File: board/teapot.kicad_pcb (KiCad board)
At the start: 2 copper layers, 49.9 x 50 mm, 47 parts, among them J1 MICROUSB, P1 BATT, P2 SMA, Q1 TEPT4400, U1 TPS79333DBVR, U2 TLV61225, U4 RFM69W, U5 STM32L052K8, U6 HTU21D, U7 MS5637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

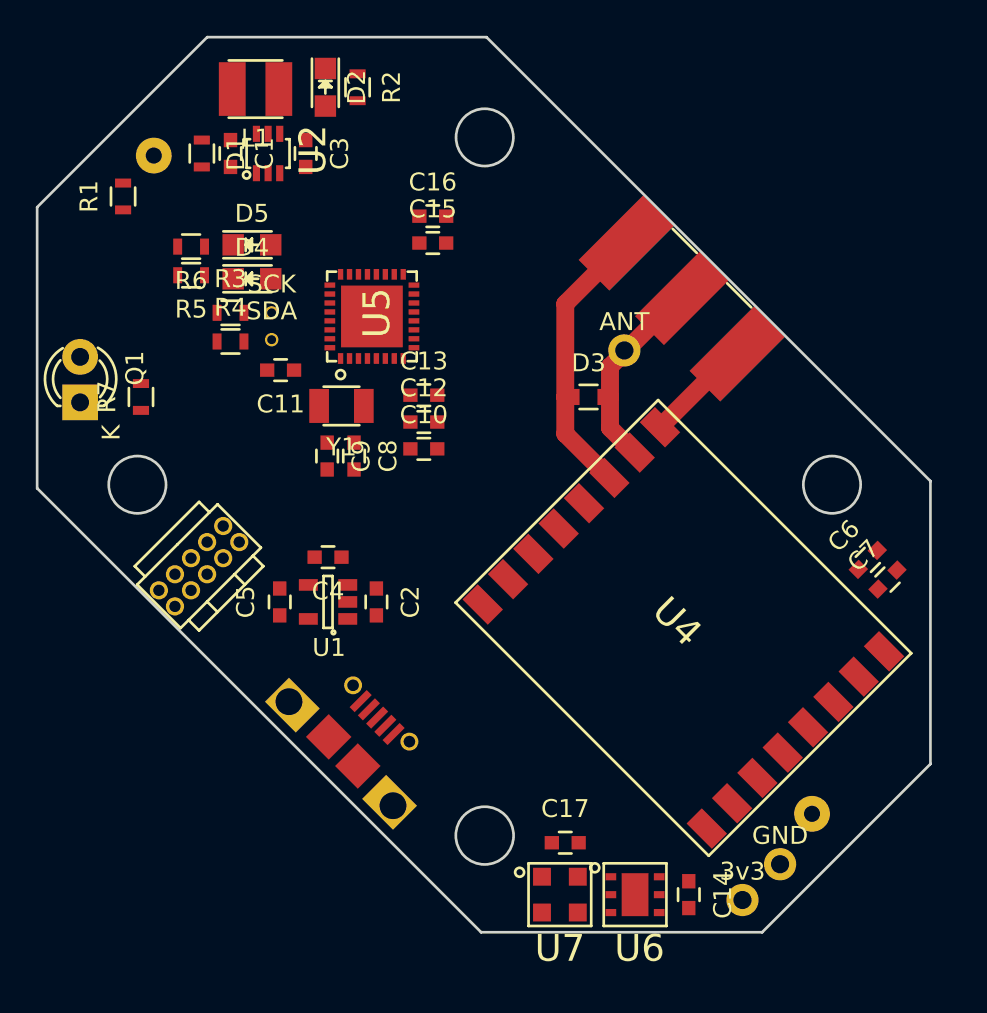
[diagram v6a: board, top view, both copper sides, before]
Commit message: layout switcher psu
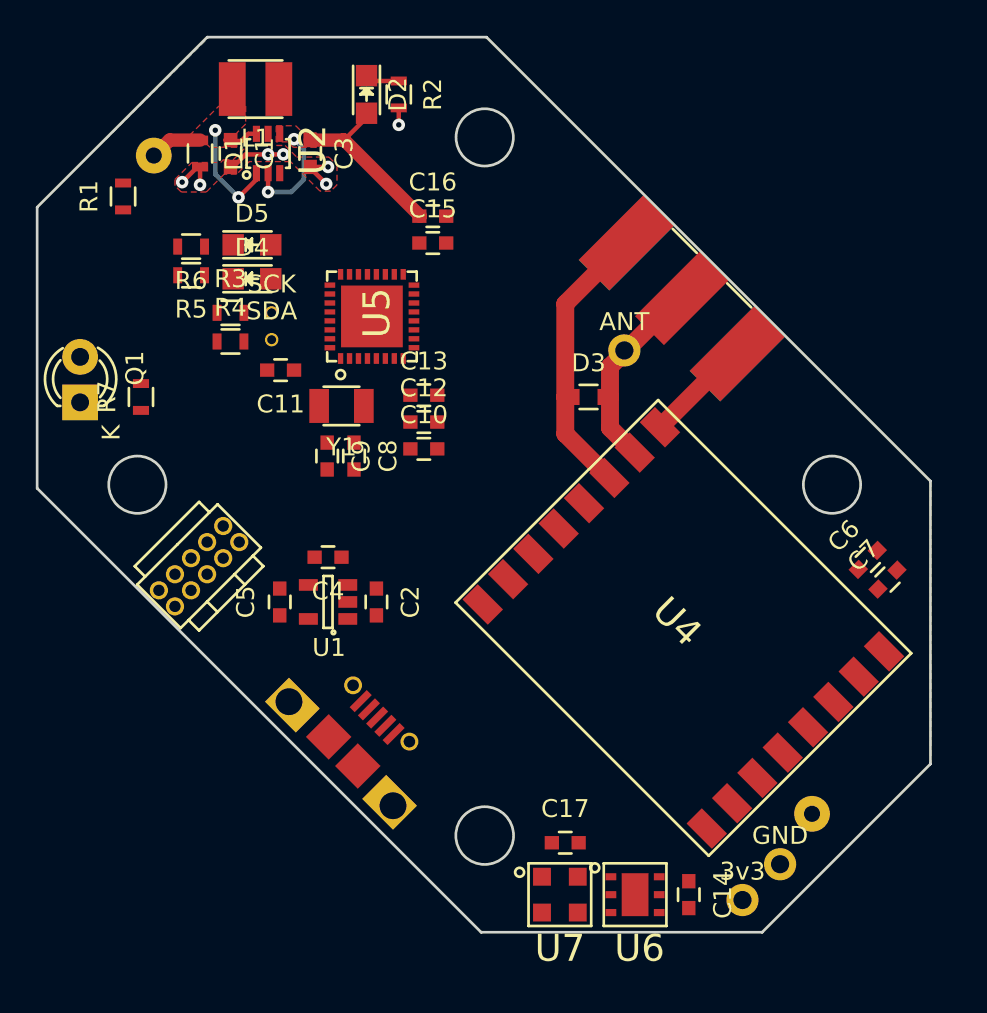
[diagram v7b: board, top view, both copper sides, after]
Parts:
- moved D2 2.33 mm to (120.4, 91.2)
- moved R2 2.33 mm to (122.2, 91.2)
- moved C3 0.25 mm to (117.2, 94.5)
- moved D1 0.10 mm to (111.1, 94.5)
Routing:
- net +3V3: track 0.00 -> 16.1 mm, vias 0 -> 2
- net Net-(C1-Pad1): track 0.00 -> 11.0 mm, vias 0 -> 2
- net GND: track 22.4 -> 31.3 mm, vias 0 -> 7
- net Net-(D2-Pad1): track 0.00 -> 2.47 mm
- added copper zone on F.Cu, net +3V3
- added copper zone on B.Cu, net GND
- added copper zone on F.Cu, net GND
- added copper zone on F.Cu, net Net-(C1-Pad1)
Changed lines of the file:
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@@
   (general
     (links 116)
-    (no_connects 111)
+    (no_connects 92)
     (area 101.924999 87.924999 151.975001 138.075001)
     (thickness 1.6)
     (drawings 16)
-    (tracks 17)
+    (tracks 73)
     (zones 0)
     (modules 47)
@@
     (user_trace_width 1)
     (trace_clearance 0.15)
-    (zone_clearance 0.5)
-    (zone_45_only no)
+    (zone_clearance 0.1)
+    (zone_45_only yes)
     (trace_min 0.2)
     (segment_width 0.2)
@@
   )
   (module Resistors_SMD:R_0603 (layer F.Cu)
-    (at 111.2 94.5 270)
+    (at 111.1 94.5 270)
     (descr "Resistor SMD 0603, reflow soldering, Vishay (see dcrcw.pdf)")
     (tags "resistor 0603")
@@
   )
   (module Capacitors_SMD:C_0603 (layer F.Cu)
-    (at 117 94.5 270)
+    (at 117.25 94.5 270)
     (descr "Capacitor SMD 0603, reflow soldering, AVX (see smccp.pdf)")
     (tags "capacitor 0603")
@@
   )
   (module LEDs:LED-0805 (layer F.Cu)
-    (at 118.1 90.8 270)
+    (at 120.4 91.2 270)
     (descr "LED 0805 smd package")
     (tags "LED 0805 SMD")
@@
   )
   (module Resistors_SMD:R_0603 (layer F.Cu)
-    (at 119.9 90.8 270)
+    (at 122.2 91.2 270)
     (descr "Resistor SMD 0603, reflow soldering, Vishay (see dcrcw.pdf)")
     (tags "resistor 0603")
@@
   (gr_circle (center 107.6 113) (end 109.2 113) (layer Edge.Cuts) (width 0.15))
   (gr_line (start 111.5 88) (end 102 97.5) (angle 90) (layer Edge.Cuts) (width 0.15))
+  (segment (start 120.4 92.24902) (end 120.4 92.5) (width 0.25) (layer F.Cu) (net 1) (status C00000))
+  (segment (start 120.4 92.5) (end 119.1 93.8) (width 0.25) (layer F.Cu) (net 1) (status 400000))
+  (segment (start 119.1 93.8) (end 119.1 93.75) (width 0.25) (layer F.Cu) (net 1))
+  (segment (start 120.3 92.3) (end 120.35 92.19902) (width 0.25) (layer F.Cu) (net 1))
+  (segment (start 117.25 93.75) (end 119.1 93.75) (width 0.75) (layer F.Cu) (net 1))
+  (segment (start 119.1 93.75) (end 119.1 93.75) (width 0.75) (layer F.Cu) (net 1))
+  (segment (start 119.1 93.75) (end 119.15 93.75) (width 0.75) (layer F.Cu) (net 1))
+  (segment (start 119.15 93.75) (end 123.4 98) (width 0.75) (layer F.Cu) (net 1))
+  (segment (start 123.4 98) (end 123.35 98) (width 0.75) (layer F.Cu) (net 1))
+  (segment (start 114.9 95.6) (end 114.9 96.65) (width 0.25) (layer F.Cu) (net 1))
+  (segment (start 116.35 93.7) (end 116.4 93.7) (width 0.25) (layer F.Cu) (net 1))
+  (via (at 116.35 93.7) (size 0.7) (drill 0.3) (layers F.Cu B.Cu) (net 1))
+  (segment (start 116.9 94.25) (end 116.35 93.7) (width 0.25) (layer B.Cu) (net 1))
+  (segment (start 116.9 95.95) (end 116.9 94.25) (width 0.25) (layer B.Cu) (net 1))
+  (segment (start 116.2 96.65) (end 116.9 95.95) (width 0.25) (layer B.Cu) (net 1))
+  (segment (start 114.9 96.65) (end 116.2 96.65) (width 0.25) (layer B.Cu) (net 1))
+  (via (at 114.9 96.65) (size 0.7) (drill 0.3) (layers F.Cu B.Cu) (net 1))
+  (segment (start 111.1 93.75) (end 109.4 93.75) (width 0.75) (layer F.Cu) (net 2))
+  (segment (start 109.4 93.75) (end 108.55 94.6) (width 0.75) (layer F.Cu) (net 2))
+  (segment (start 108.55 94.6) (end 108.515224 94.615224) (width 0.75) (layer F.Cu) (net 2))
+  (segment (start 114.25 95.6) (end 114.25 95.95) (width 0.25) (layer F.Cu) (net 2))
+  (segment (start 114.25 95.95) (end 113.25 96.95) (width 0.25) (layer F.Cu) (net 2))
+  (via (at 111.95 93.2) (size 0.7) (drill 0.3) (layers F.Cu B.Cu) (net 2))
+  (segment (start 111.95 95.65) (end 111.95 93.2) (width 0.25) (layer B.Cu) (net 2))
+  (segment (start 113.25 96.95) (end 111.95 95.65) (width 0.25) (layer B.Cu) (net 2))
+  (via (at 113.25 96.95) (size 0.7) (drill 0.3) (layers F.Cu B.Cu) (net 2))
+  (segment (start 112.8 93.75) (end 112.5 93.75) (width 0.25) (layer F.Cu) (net 2))
+  (segment (start 114.25 95.55) (end 114.25 95.6) (width 0.25) (layer F.Cu) (net 2))
+  (segment (start 114.25 93.4) (end 113.8 93.4) (width 0.25) (layer F.Cu) (net 2))
+  (segment (start 113.4 93.8) (end 112.8 93.8) (width 0.25) (layer F.Cu) (net 2))
+  (segment (start 113.8 93.4) (end 113.4 93.8) (width 0.25) (layer F.Cu) (net 2))
+  (segment (start 112.8 93.8) (end 112.8 93.75) (width 0.25) (layer F.Cu) (net 2))
+  (segment (start 122.2 91.95) (end 122.2 92.9) (width 0.25) (layer F.Cu) (net 3) (status 400000))
+  (via (at 122.2 92.9) (size 0.7) (drill 0.3) (layers F.Cu B.Cu) (net 3))
+  (segment (start 117.25 95.25) (end 117.25 95.3) (width 0.25) (layer F.Cu) (net 3))
+  (segment (start 117.25 95.3) (end 118.15 96.2) (width 0.25) (layer F.Cu) (net 3))
+  (via (at 118.15 96.2) (size 0.7) (drill 0.3) (layers F.Cu B.Cu) (net 3))
+  (segment (start 117.25 95.25) (end 118.25 95.25) (width 0.25) (layer F.Cu) (net 3))
+  (via (at 118.25 95.25) (size 0.7) (drill 0.3) (layers F.Cu B.Cu) (net 3))
+  (segment (start 111.1 95.25) (end 110.95 95.25) (width 0.25) (layer F.Cu) (net 3))
+  (segment (start 110.95 95.25) (end 110.1 96.1) (width 0.25) (layer F.Cu) (net 3))
+  (via (at 110.1 96.1) (size 0.7) (drill 0.3) (layers F.Cu B.Cu) (net 3))
+  (segment (start 111.1 95.25) (end 111.1 96.25) (width 0.25) (layer F.Cu) (net 3))
+  (via (at 111.1 96.25) (size 0.7) (drill 0.3) (layers F.Cu B.Cu) (net 3))
+  (segment (start 114.95 94.55) (end 114.9 94.55) (width 0.25) (layer F.Cu) (net 3))
+  (via (at 114.9 94.55) (size 0.7) (drill 0.3) (layers F.Cu B.Cu) (net 3))
+  (segment (start 112.8 95.25) (end 112.95 95.25) (width 0.25) (layer F.Cu) (net 3))
+  (segment (start 112.95 95.25) (end 113.65 94.55) (width 0.25) (layer F.Cu) (net 3))
+  (segment (start 113.65 94.55) (end 114.95 94.55) (width 0.25) (layer F.Cu) (net 3))
+  (segment (start 114.95 94.55) (end 115.75 94.55) (width 0.25) (layer F.Cu) (net 3))
+  (via (at 115.75 94.55) (size 0.7) (drill 0.3) (layers F.Cu B.Cu) (net 3))
   (segment (start 132.05 108.1) (end 131.6 108.1) (width 0.25) (layer F.Cu) (net 3))
   (segment (start 131.6 108.1) (end 131.5 108.1) (width 0.25) (layer F.Cu) (net 3))
@@
   (segment (start 131.5 108.1) (end 131.5 102.9) (width 1) (layer F.Cu) (net 3))
   (segment (start 135 99.4) (end 134.901812 99.501812) (width 1) (layer F.Cu) (net 3))
+  (segment (start 122.2 90.45) (end 120.45 90.45) (width 0.25) (layer F.Cu) (net 15) (status C00000))
+  (segment (start 120.45 90.45) (end 120.4 90.4) (width 0.25) (layer F.Cu) (net 15) (status C00000))
+  (segment (start 120.4 90.4) (end 120.4 90.15098) (width 0.25) (layer F.Cu) (net 15) (status C00000))
+  (segment (start 120.25 90.45) (end 120.2 90.4) (width 0.25) (layer F.Cu) (net 15))
+  (segment (start 120.2 90.4) (end 120.35 90.10098) (width 0.25) (layer F.Cu) (net 15))
   (segment (start 133.55 108.1) (end 134.1 108.1) (width 0.25) (layer F.Cu) (net 16))
   (segment (start 134.1 108.1) (end 134 108.1) (width 0.25) (layer F.Cu) (net 16))
@@
   (segment (start 134 108.1) (end 134 106.4) (width 1) (layer F.Cu) (net 16))
   (segment (start 138 102.4) (end 138 102.6) (width 1) (layer F.Cu) (net 16))
+  (zone (net 3) (net_name GND) (layer B.Cu) (hatch edge 0.508)
+    (connect_pads (clearance 0.25))
+    (min_thickness 0.25)
+    (fill yes (arc_segments 16) (thermal_gap 0.25) (thermal_bridge_width 0.26))
+    (polygon
+      (pts
+        (xy 111.6 88) (xy 127.1 88) (xy 151.9 112.8) (xy 151.9 128.6) (xy 142.5 138)
+        (xy 126.8 138) (xy 102 113.2) (xy 102 97.5) (xy 111.6 88)
+      )
+    )
+  )
+  (zone (net 3) (net_name GND) (layer F.Cu) (hatch edge 0.508)
+    (connect_pads yes (clearance 0.1))
+    (min_thickness 0.1)
+    (fill yes (arc_segments 16) (thermal_gap 0.25) (thermal_bridge_width 0.26))
+    (polygon
+      (pts
+        (xy 116.5 94.7) (xy 118.3 94.7) (xy 118.75 95.15) (xy 118.75 96.25) (xy 118.4 96.6)
+        (xy 117.8 96.6) (xy 116.15 94.95) (xy 113.85 94.95) (xy 113.15 95.65) (xy 112.45 95.65)
+        (xy 111.45 96.65) (xy 110.05 96.65) (xy 109.7 96.3) (xy 109.7 95.95) (xy 110.65 95)
+        (xy 112.25 95) (xy 112.4 94.85) (xy 112.95 94.85) (xy 113.75 94.05) (xy 115.85 94.05)
+        (xy 116.5 94.7)
+      )
+    )
+  )
+  (zone (net 2) (net_name "Net-(C1-Pad1)") (layer F.Cu) (hatch edge 0.508)
+    (connect_pads yes (clearance 0.1))
+    (min_thickness 0.1)
+    (fill yes (arc_segments 16) (thermal_gap 0.25) (thermal_bridge_width 0.26))
+    (polygon
+      (pts
+        (xy 113.65 92.85) (xy 113.15 93.35) (xy 113.15 94.15) (xy 111.65 94.15) (xy 111.5 94)
+        (xy 110.5 94) (xy 110.5 93.5) (xy 112.15 91.85) (xy 113.65 91.85) (xy 113.65 92.85)
+      )
+    )
+  )
+  (zone (net 1) (net_name +3V3) (layer F.Cu) (hatch edge 0.508)
+    (connect_pads yes (clearance 0.1))
+    (min_thickness 0.1)
+    (fill yes (arc_segments 16) (thermal_gap 0.25) (thermal_bridge_width 0.26))
+    (polygon
+      (pts
+        (xy 116.85 93.35) (xy 117.6 93.35) (xy 117.6 94.15) (xy 116.3 94.15) (xy 116 93.85)
+        (xy 115.35 93.85) (xy 115.35 92.95) (xy 116.45 92.95) (xy 116.85 93.35)
+      )
+    )
+  )
 )

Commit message: Routed 3v3 and some GND.
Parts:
- moved C2 8.24 mm to (113.3, 122.6), turned to 315 degrees
- moved C14 4.47 mm to (135.5, 132.5), turned to 180 degrees
- moved U1 2.91 mm to (115.5, 120.5), turned to 45 degrees
- moved C5 2.56 mm to (117.2, 117.5), turned to 45 degrees
- moved C4 1.82 mm to (118.5, 118.8), turned to 45 degrees
- moved U6 0.73 mm to (135.6, 135.2), turned to 90 degrees
- moved Y1 0.11 mm to (119.0, 108.7)
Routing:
- net +3V3: track 16.1 -> 139.6 mm
- net GND: track 31.3 -> 46.7 mm, vias 7 -> 20
- net +5V: track 0.00 -> 11.7 mm
- net Net-(C9-Pad1): track 0.00 -> 6.54 mm
- net /nRST: track 0.00 -> 6.42 mm
- net Net-(C8-Pad1): track 0.00 -> 5.48 mm
- net Net-(C4-Pad1): track 0.00 -> 1.45 mm
